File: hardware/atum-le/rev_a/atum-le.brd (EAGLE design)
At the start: 18.8 x 19.6 mm, 40 parts, among them J1 TC2030-JLINK-NL, J2 SH_MALE_2/1MM, J3 ATUM-HEADER, U2 FM25LBTDFN-8, U3 RV-3049-C3, U4 TPS62740, U5 NRF51822QF, X1 EPSON-FA-128, X2 ABS05-32.768KHZ-T

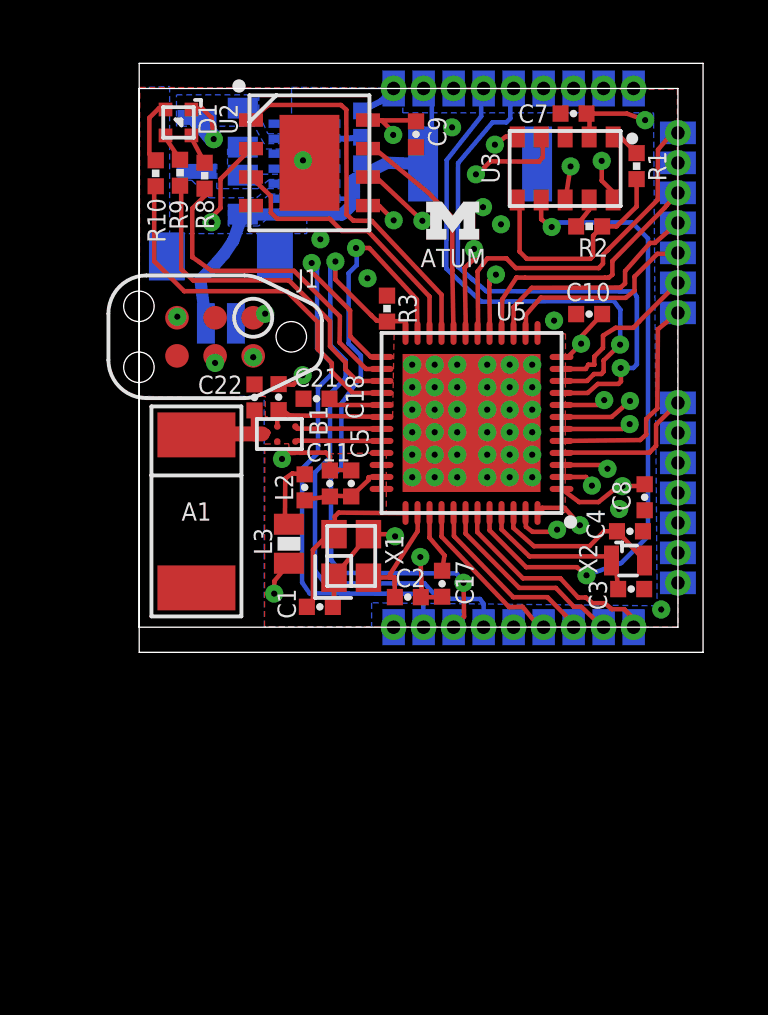
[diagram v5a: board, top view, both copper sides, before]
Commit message: moved a few vias
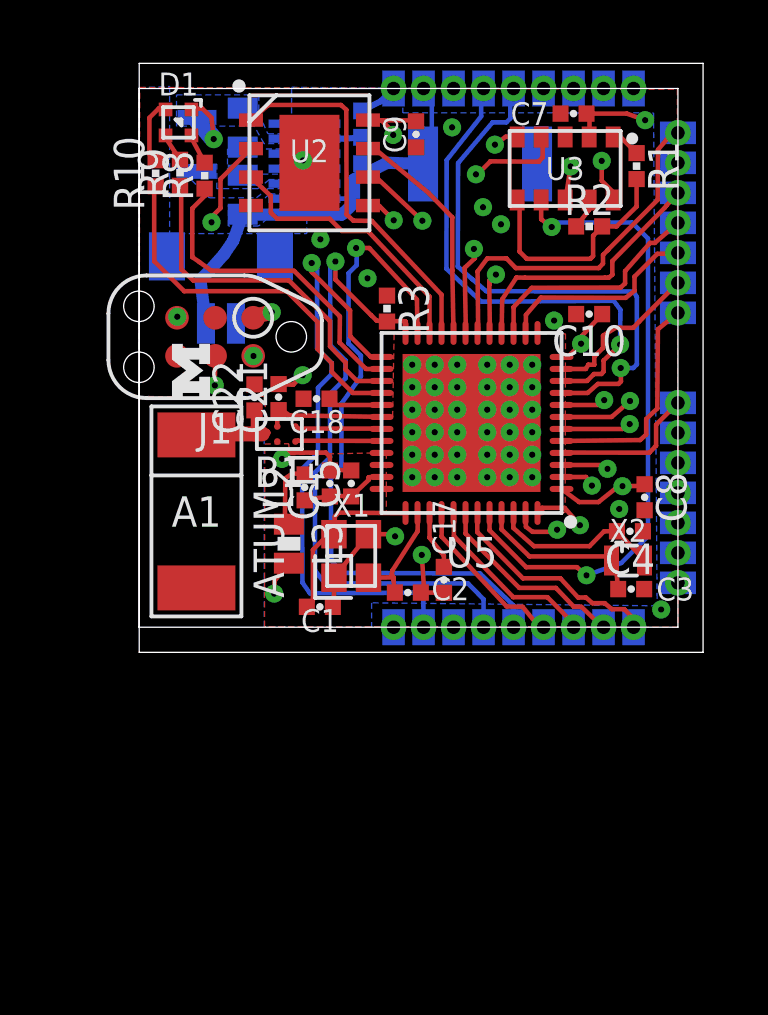
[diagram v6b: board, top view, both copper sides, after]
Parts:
- moved LOGO1 10.1 mm to (1.73, 8.56), turned to 90 degrees
- moved C2 0.15 mm to (8.95, 1.15)
- moved C17 0.14 mm to (10.2, 1.58)
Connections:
- removed net UNUSED1: J3.5, J3.5B
- removed net UNUSED2: J3.10, J3.10B
- removed net UNUSED3: J3.11, J3.11B
- removed net UNUSED4: J3.12, J3.12B
- removed net UNUSED5: J3.13, J3.13B
- new net N$1: J3.30, J3.30B
- net SWDIO/!RESET: now also J3.5, J3.5B; no longer J3.3, J3.30, J3.30B, J3.3B
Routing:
- net SWDIO/!RESET: track 36.0 -> 29.0 mm, vias 3 -> 2
- net SWDCLK: track 29.0 -> 30.5 mm
- net N$38: track 17.1 -> 16.5 mm
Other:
- board text added: "2015/02/23"
- board text added: "Brad Campbell"
- board text removed: "2015/004/20"
- board text removed: "Joshua Adkins Brad Campbell"

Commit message: finished routing cleanup and silk
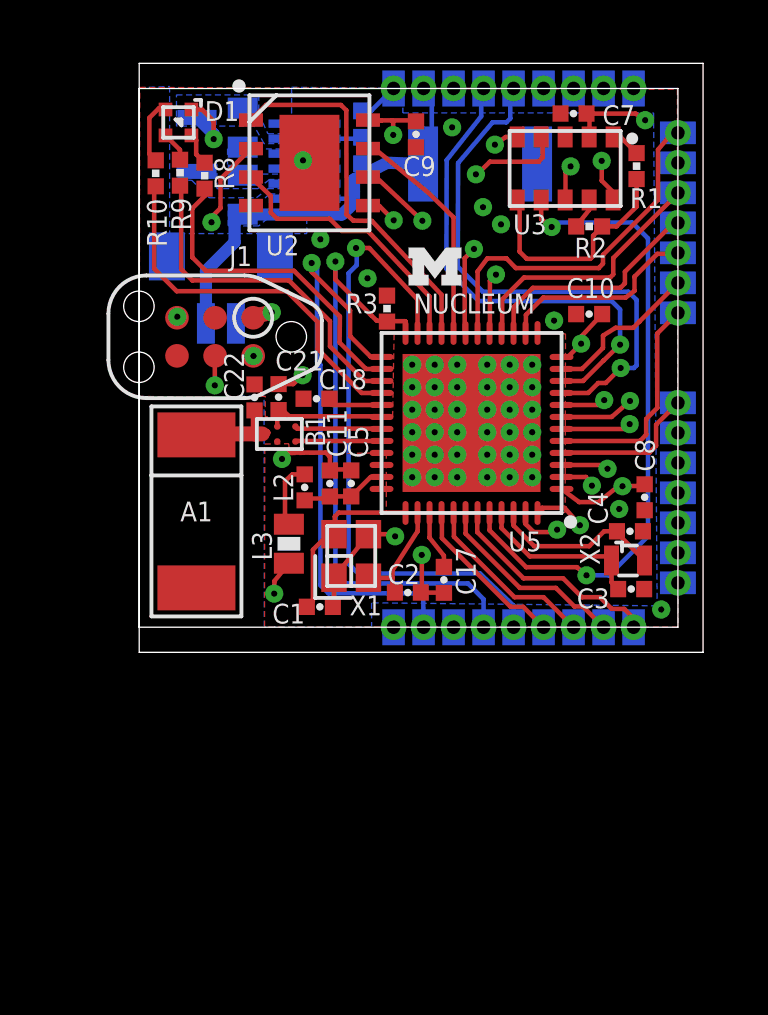
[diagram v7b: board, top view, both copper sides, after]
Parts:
- moved LOGO1 8.84 mm to (9.86, 12.0), turned to 0 degrees
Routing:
- net SWDCLK: track 30.5 -> 29.1 mm
- net P17: track 20.9 -> 19.8 mm
- net SPI_MISO: track 36.8 -> 35.7 mm
- net SWDIO/!RESET: track 29.0 -> 28.0 mm
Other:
- board text added: "2015/04/20"
- board text added: "Joshua Adkins Brad Campbell"
- board text added: "NUCLEUM"
- board text removed: "2015/02/23"
- board text removed: "ATUM"
- board text removed: "Brad Campbell"
